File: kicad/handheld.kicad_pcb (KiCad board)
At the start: 4 copper layers, 240 x 77.7 mm, 128 parts, among them J1 Conn_01x08, J2 61300311121, J3 AVR-PDI-6, J4 UE27AC54100, Q1 PN2222A, SW1 HOLD, SW10 SELECT, SW2 PAUSE, SW3 SDROP, SW4 HDROP, SW5 ROTR, SW6 RIGHT, SW7 ROTL, SW8 RIGHT, SW9 START, U1 TFBS4711, U10 DMN601, U11 NSI45015, U12 SN74LV573, U13 P-FET, U14 NSI45015, U15 DMN601, U16 NSI45015, U17 NSI45015, U18 DMN601, U19 P-FET, U2 ATxmega64C3-AU, U20 NSI45015, U21 74HCT595, U22 NSI45015, U23 DMN601, U24 NSI45015, U25 P-FET, U26 NSI45015, U27 DMN601, U28 NSI45015, U29 SN74LV573, U3 P-FET, U30 NSI45015, U31 DMN601, U32 NSI45015, U33 P-FET, U34 NSI45015, U35 DMN601, U36 NSI45015, U37 NSI45015, U38 P-FET, U39 DMN601, U4 LM3671MF-3.3, U40 NSI45015, U41 NSI45015, U42 DMN601, U43 NSI45015, U44 SN74LV573, U45 74HCT595, U46 P-FET, U47 NSI45015, U48 DMN601, U49 NSI45015, U5 NSI45015, U50 NSI45015, U51 DMN601, U52 P-FET, U53 NSI45015, U54 SN74LVC1G08DBVR, U55 SN74LVC1G08DBVR, U56 SN74LVC1G08DBVR, U57 SN74LVC1G08DBVR, U6 P-FET, U7 DMN601, U8 NSI45015, U9 NSI45015

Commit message: Disconnect USB shield from ground plane
Also Fixed obscured refdes indicators.
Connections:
- J4 pad SH: GND -> Net-(J4-PadSH)
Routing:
- net Net-(J4-PadSH): track 0.00 -> 14.5 mm
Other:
- board text added: "v0.2 01/2021"
- board text removed: "v0.1 12/2020"

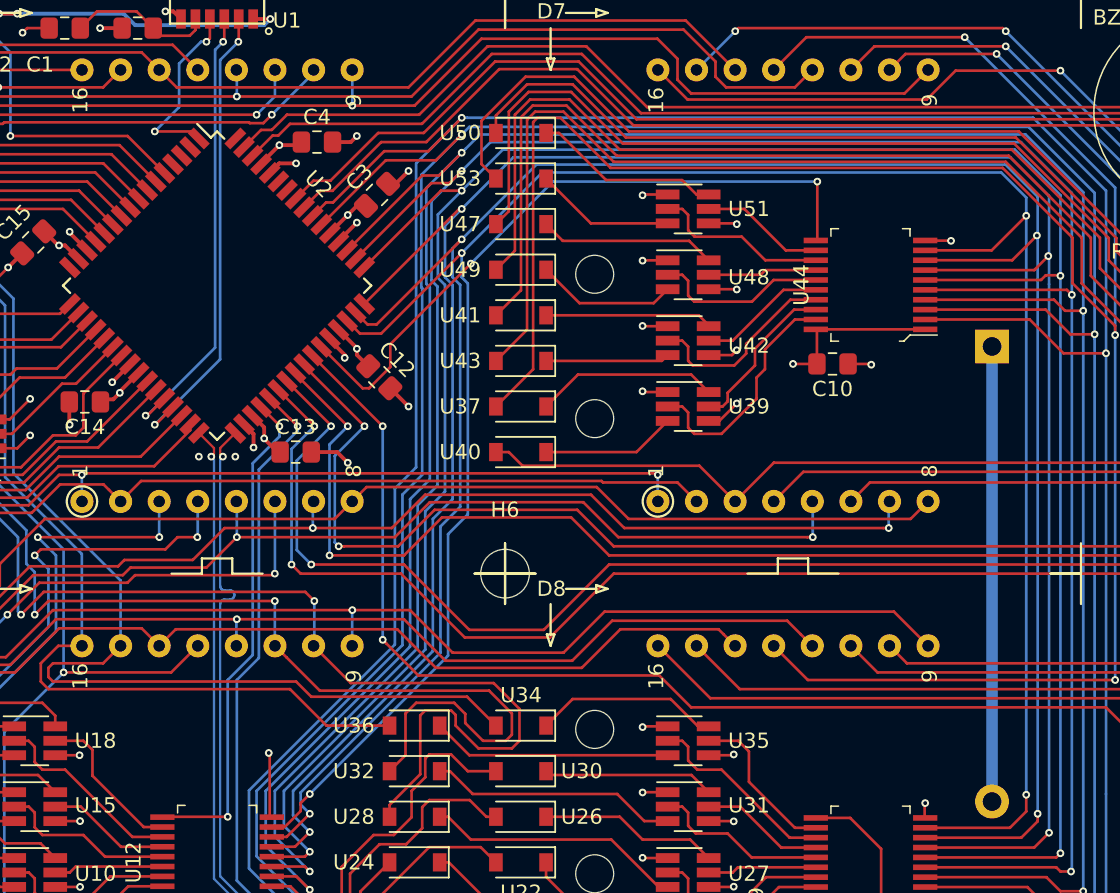
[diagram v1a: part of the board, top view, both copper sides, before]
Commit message: Draw outlines for 74lv273 castellated shield
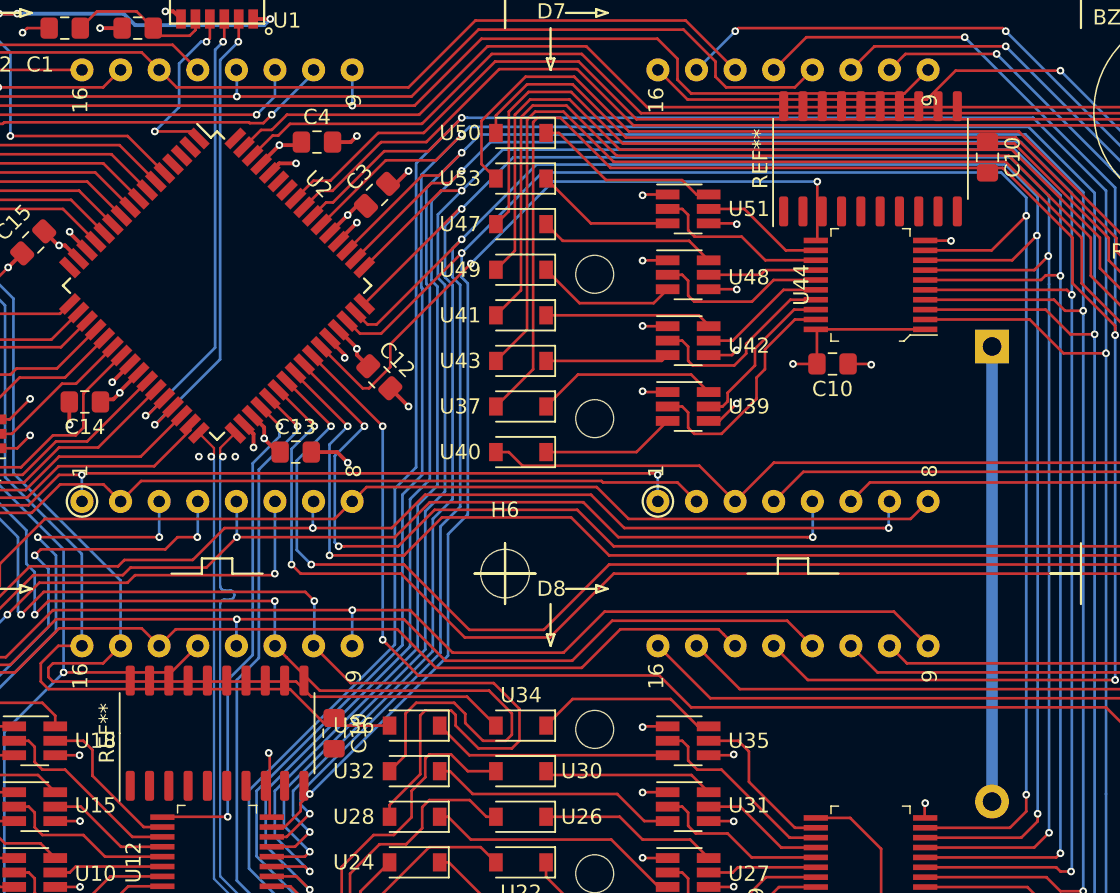
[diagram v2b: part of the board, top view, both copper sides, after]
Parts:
- added C10: 100nF, Capacitor_SMD:C_0805_2012Metric_Pad1.15x1.40mm_HandSolder, F.Cu at (160.1, 112.1)
- added C10: 100nF, Capacitor_SMD:C_0805_2012Metric_Pad1.15x1.40mm_HandSolder, F.Cu at (203.1, 74.2)
- added REF**: SO-20_5.3x12.6mm_P1.27mm, Package_SO:SO-20_5.3x12.6mm_P1.27mm, F.Cu at (152.4, 112.1)
- added REF**: SO-20_5.3x12.6mm_P1.27mm, Package_SO:SO-20_5.3x12.6mm_P1.27mm, F.Cu at (195.4, 74.3)

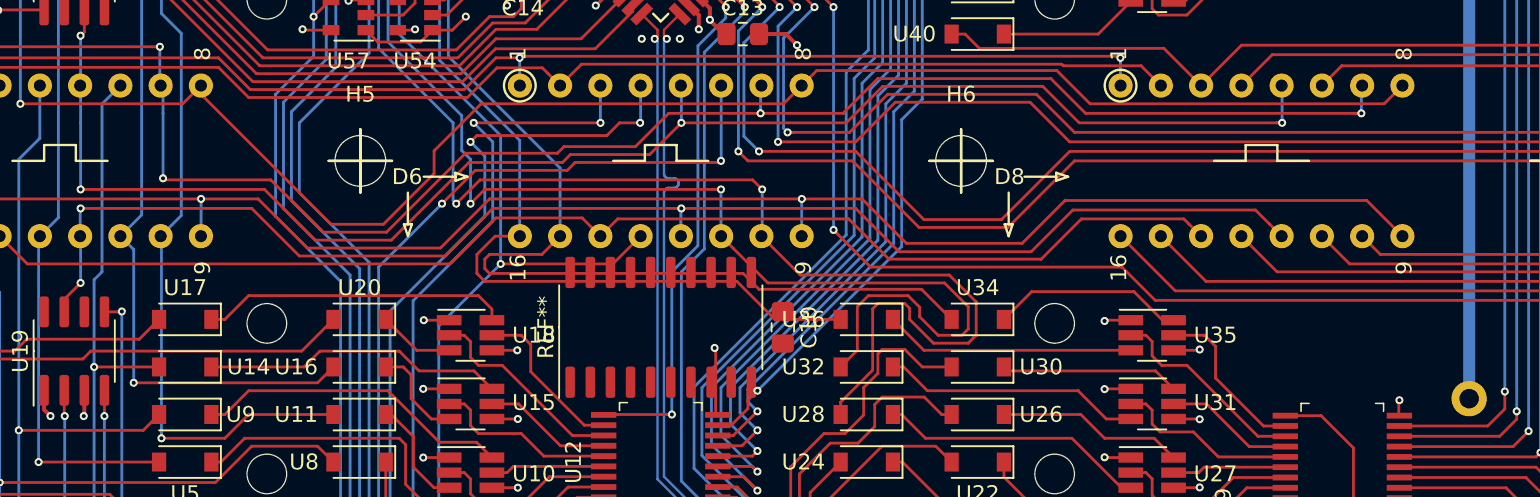
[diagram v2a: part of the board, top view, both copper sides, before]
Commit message: Adds errata shield PCB for messed up SSOP-20 pinout
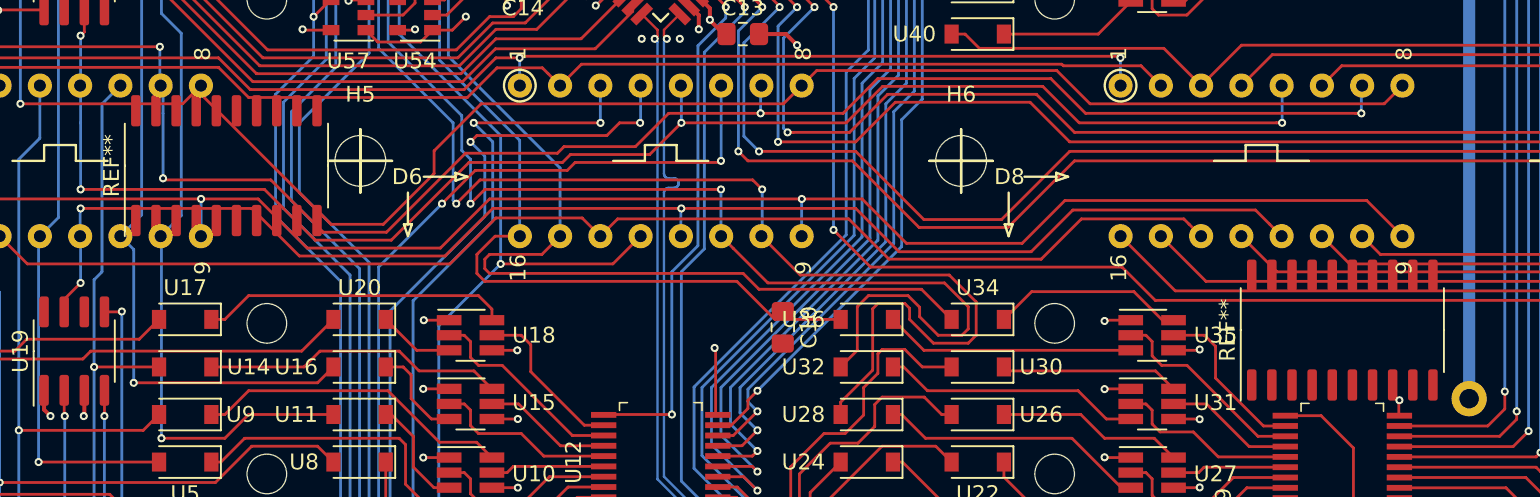
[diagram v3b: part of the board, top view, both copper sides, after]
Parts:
- removed the REF** at (152.4, 112.1)
- added REF**: SO-20_5.3x12.6mm_P1.27mm, Package_SO:SO-20_5.3x12.6mm_P1.27mm, F.Cu at (125.0, 101.9)
- added REF**: SO-20_5.3x12.6mm_P1.27mm, Package_SO:SO-20_5.3x12.6mm_P1.27mm, F.Cu at (195.4, 112.3)

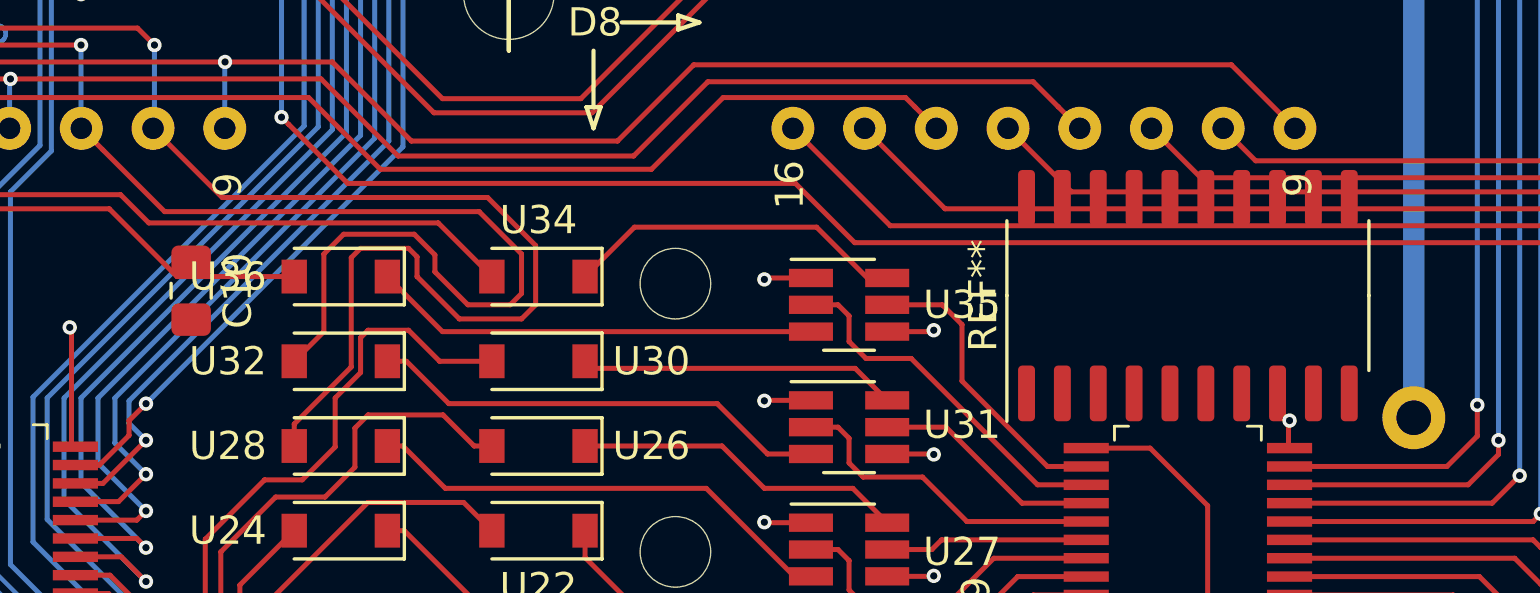
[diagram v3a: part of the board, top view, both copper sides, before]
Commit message: Remove shield measurements
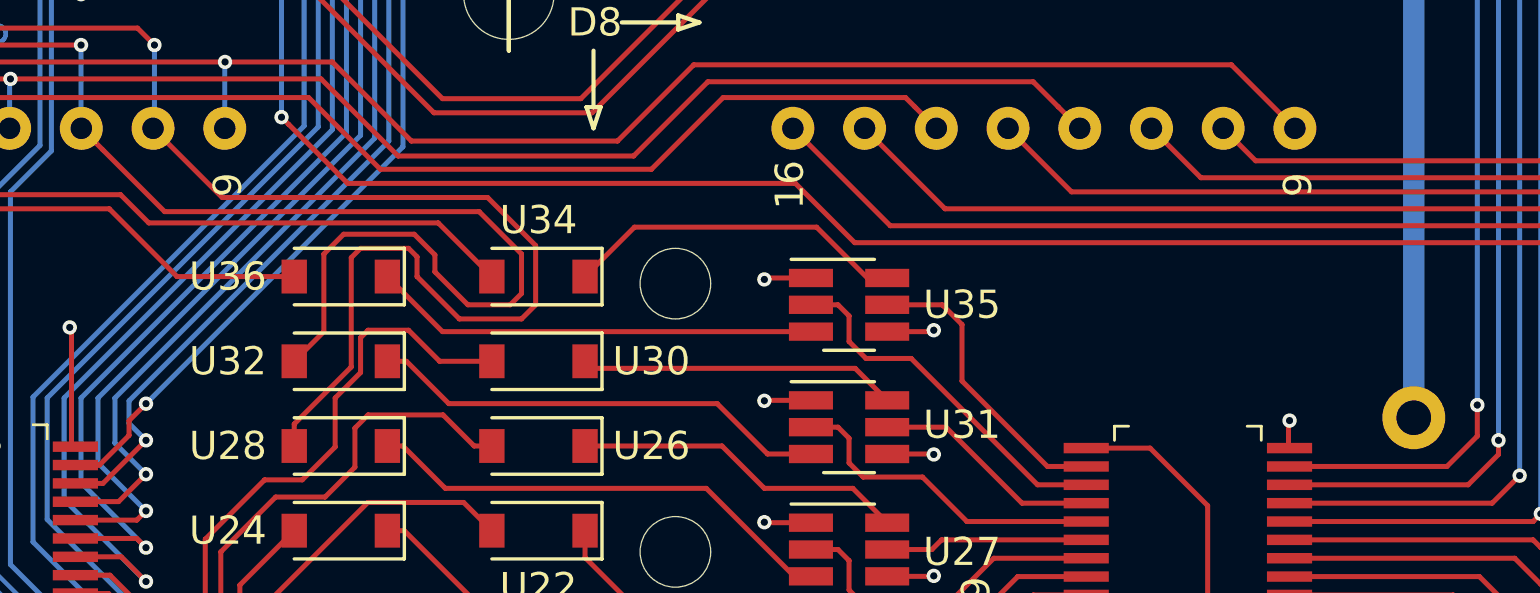
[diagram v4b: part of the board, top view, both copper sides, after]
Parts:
- removed the C10 at (160.1, 112.1)
- removed the REF** at (195.4, 112.3)
